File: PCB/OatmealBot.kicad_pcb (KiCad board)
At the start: 2 copper layers, 65 x 56 mm, 5 parts, among them J2 RPi_GPIO

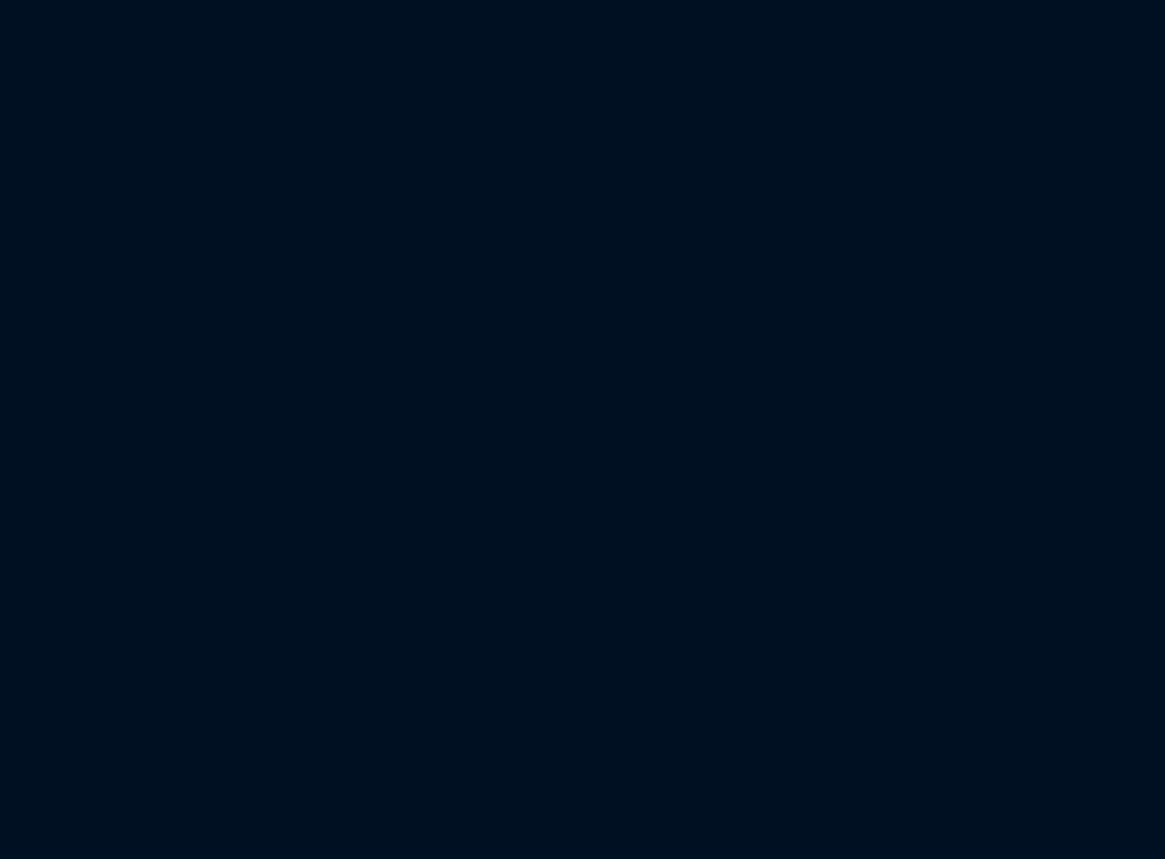
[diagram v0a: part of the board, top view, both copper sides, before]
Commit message: Started assigning some footprints. Initial PCB layout.
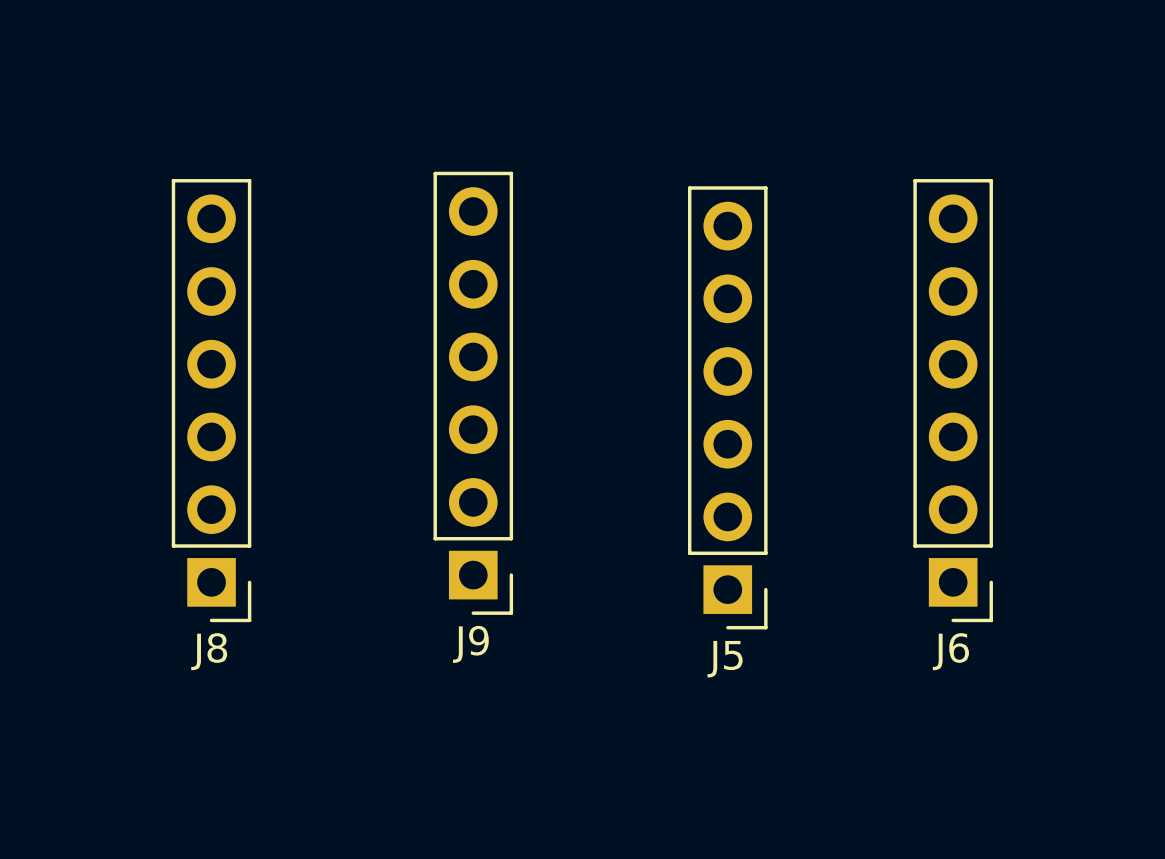
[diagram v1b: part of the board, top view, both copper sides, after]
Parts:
- added J5: Motor 3, Pin_Headers:Pin_Header_Straight_1x06_Pitch2.54mm, F.Cu at (53.3, 67.3)
- added J6: Motor 4, Pin_Headers:Pin_Header_Straight_1x06_Pitch2.54mm, F.Cu at (61.2, 67.1)
- added J8: Motor 1, Pin_Headers:Pin_Header_Straight_1x06_Pitch2.54mm, F.Cu at (35.3, 67.1)
- added J9: Motor 2, Pin_Headers:Pin_Header_Straight_1x06_Pitch2.54mm, F.Cu at (44.5, 66.8)
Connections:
- net Net-(J2-Pad1) renamed +3.3V
- net Net-(J2-Pad10) renamed PI_RXD
- net Net-(J2-Pad11) renamed Servo3
- net Net-(J2-Pad12) renamed Servo2
- net Net-(J2-Pad18) renamed OLED_RESET
- net Net-(J2-Pad19) renamed MOSI
- net Net-(J2-Pad21) renamed MISO
- net Net-(J2-Pad22) renamed OLED_DC
- net Net-(J2-Pad23) renamed SCLK
- net Net-(J2-Pad24) renamed OLED_CS
- net Net-(J2-Pad29) renamed ENC4B
- net Net-(J2-Pad31) renamed ENC4A
- net Net-(J2-Pad32) renamed Servo1
- net Net-(J2-Pad33) renamed ENC3A
- net Net-(J2-Pad35) renamed ENC3B
- net Net-(J2-Pad36) renamed ENC2A
- net Net-(J2-Pad37) renamed ENC2B
- net Net-(J2-Pad38) renamed ENC1B
- net Net-(J2-Pad40) renamed ENC1A
- net Net-(J2-Pad8) renamed PI_TXD
- J2 pad 14: Net-(J2-Pad14) -> GND
- J2 pad 2: Net-(J2-Pad2) -> +5V
- J2 pad 20: Net-(J2-Pad20) -> GND
- J2 pad 25: Net-(J2-Pad25) -> GND
- J2 pad 30: Net-(J2-Pad30) -> GND
- J2 pad 34: Net-(J2-Pad34) -> GND
- J2 pad 39: Net-(J2-Pad39) -> GND
- J2 pad 4: Net-(J2-Pad4) -> +5V
- J2 pad 6: Net-(J2-Pad6) -> GND
- J2 pad 9: Net-(J2-Pad9) -> GND

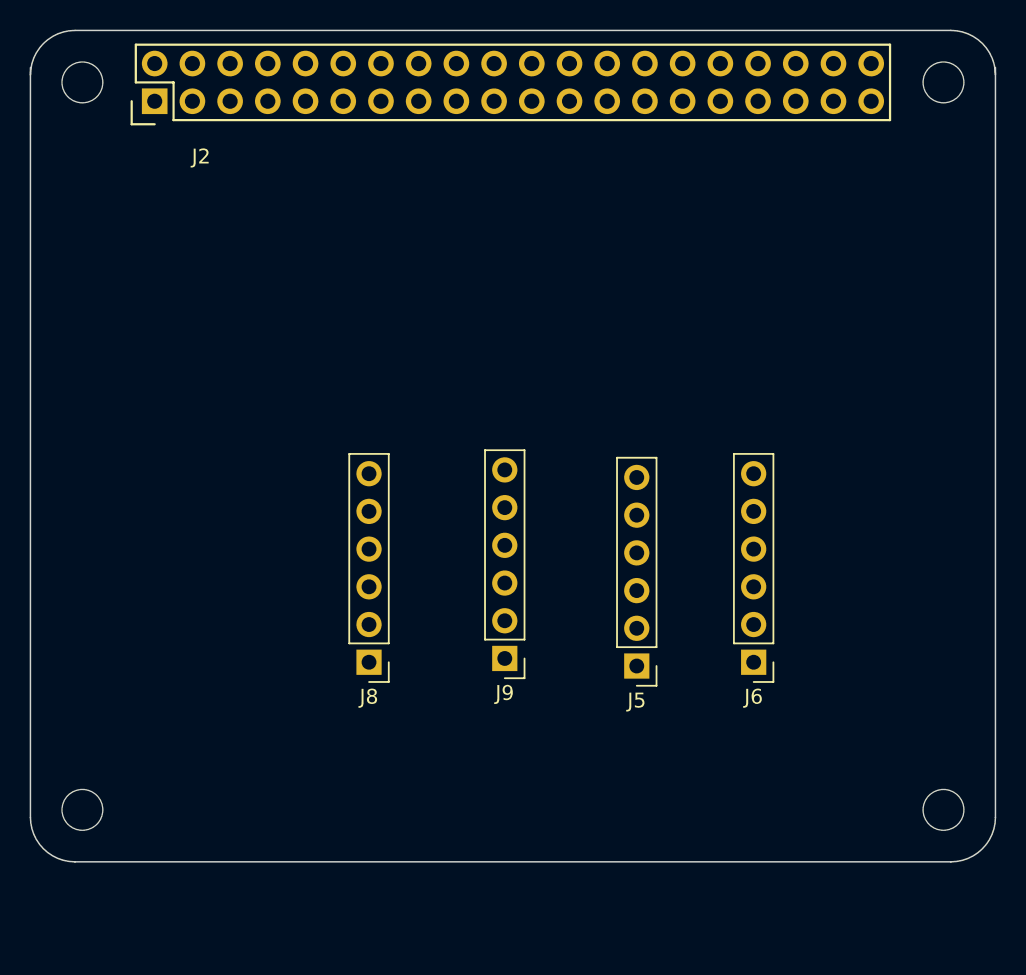
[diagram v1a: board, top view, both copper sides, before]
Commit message: Fixed PCB edges to connect properly. Removed extra explanation text about selecting the right footprint. Attempted to fix 3D models, but it hasn't worked right.
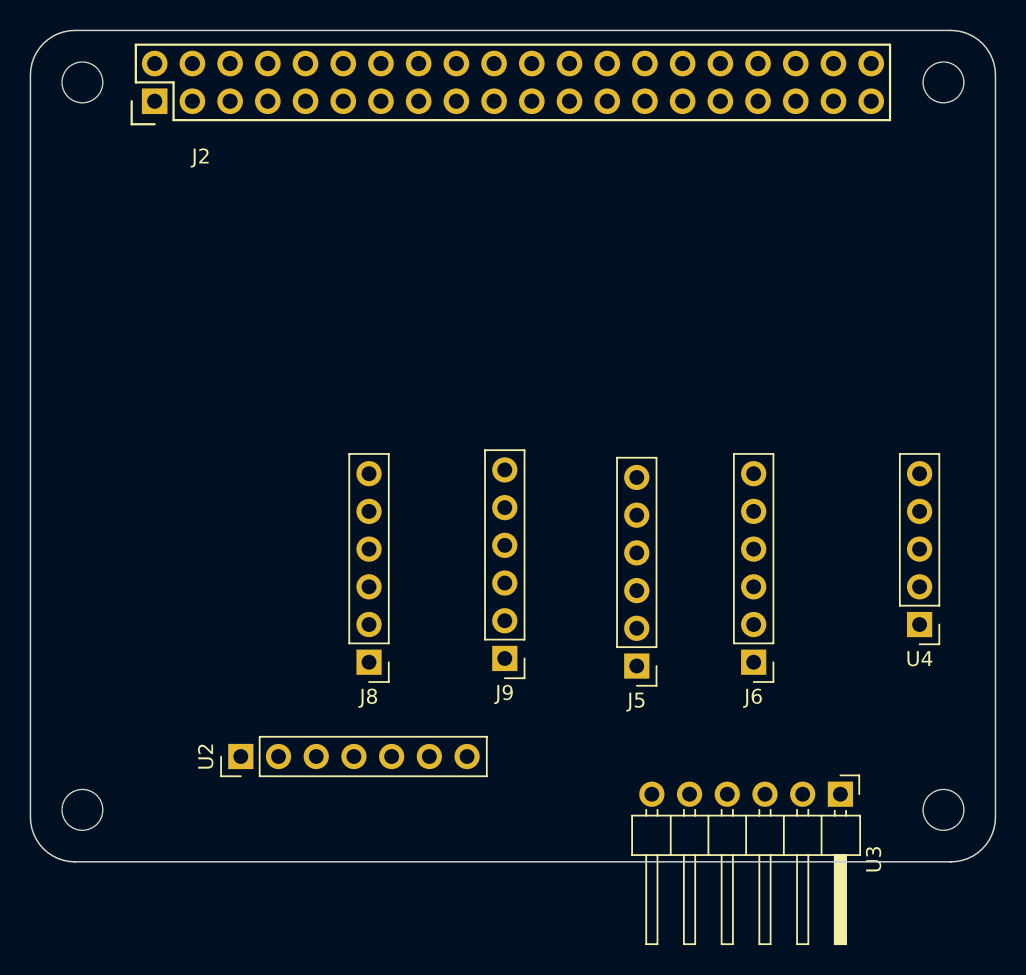
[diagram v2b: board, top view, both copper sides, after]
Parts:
- added U2: SPI_OLED, Socket_Strips:Socket_Strip_Straight_1x07_Pitch2.54mm, F.Cu at (26.7, 73.4)
- added U3: FTDI-Cable, Pin_Headers:Pin_Header_Angled_1x06_Pitch2.54mm, F.Cu at (67.1, 75.9)
- added U4: PololuD24V22F, Socket_Strips:Socket_Strip_Straight_1x05_Pitch2.54mm, F.Cu at (72.4, 64.5)
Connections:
- net Net-(J2-Pad13) renamed HighPower2
- net Net-(J2-Pad7) renamed Headlight
- J2 pad 17: Net-(J2-Pad17) -> +3.3V
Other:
- outline, holes or cut-outs redrawn
- board text removed: "Select one of these board edges depending upon the type of socket that is used."

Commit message: Fixed some of the 3D models. SPI_OLED and the Pololu power connector still aren't lined up properly though.
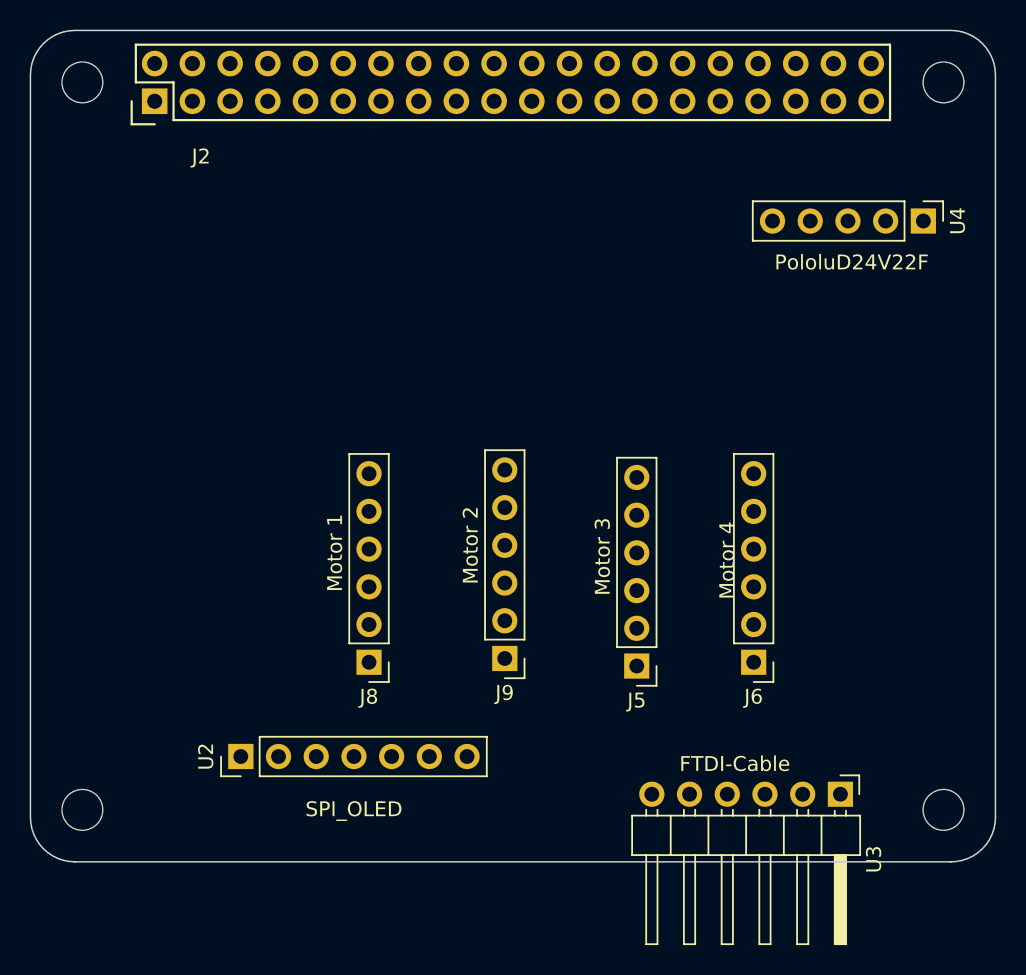
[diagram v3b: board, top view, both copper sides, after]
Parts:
- moved U4 27.2 mm to (72.6, 37.3), turned to 270 degrees
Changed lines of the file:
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@@
       (effects (font (size 1 1) (thickness 0.15)))
     )
-    (fp_text value "Motor 3" (at 0 15.03 180) (layer F.Fab)
+    (fp_text value "Motor 3" (at 2.286 7.366 270) (layer F.SilkS)
       (effects (font (size 1 1) (thickness 0.15)))
     )
@@
     (pad 6 thru_hole oval (at 0 12.7 180) (size 1.7 1.7) (drill 1) (layers *.Cu *.Mask)
       (net 33 "Net-(J5-Pad6)"))
-    (model ${KISYS3DMOD}/Pin_Headers.3dshapes/Pin_Header_Straight_1x06_Pitch2.54mm.wrl
+    (model ${KISYS3DMOD}/Connector_PinHeader_2.54mm.3dshapes/PinHeader_1x06_P2.54mm_Vertical.wrl
       (at (xyz 0 0 0))
       (scale (xyz 1 1 1))
@@
       (effects (font (size 1 1) (thickness 0.15)))
     )
-    (fp_text value "Motor 4" (at 0 15.03 180) (layer F.Fab)
+    (fp_text value "Motor 4" (at 1.778 6.858 270) (layer F.SilkS)
       (effects (font (size 1 1) (thickness 0.15)))
     )
@@
     (pad 6 thru_hole oval (at 0 12.7 180) (size 1.7 1.7) (drill 1) (layers *.Cu *.Mask)
       (net 37 "Net-(J6-Pad6)"))
-    (model ${KISYS3DMOD}/Pin_Headers.3dshapes/Pin_Header_Straight_1x06_Pitch2.54mm.wrl
+    (model ${KISYS3DMOD}/Connector_PinHeader_2.54mm.3dshapes/PinHeader_1x06_P2.54mm_Vertical.wrl
       (at (xyz 0 0 0))
       (scale (xyz 1 1 1))
@@
       (effects (font (size 1 1) (thickness 0.15)))
     )
-    (fp_text value "Motor 1" (at 0 15.03 180) (layer F.Fab)
+    (fp_text value "Motor 1" (at 2.286 7.366 270) (layer F.SilkS)
       (effects (font (size 1 1) (thickness 0.15)))
     )
@@
     (pad 6 thru_hole oval (at 0 12.7 180) (size 1.7 1.7) (drill 1) (layers *.Cu *.Mask)
       (net 41 "Net-(J8-Pad6)"))
-    (model ${KISYS3DMOD}/Pin_Headers.3dshapes/Pin_Header_Straight_1x06_Pitch2.54mm.wrl
+    (model ${KISYS3DMOD}/Connector_PinHeader_2.54mm.3dshapes/PinHeader_1x06_P2.54mm_Vertical.wrl
       (at (xyz 0 0 0))
       (scale (xyz 1 1 1))
@@
       (effects (font (size 1 1) (thickness 0.15)))
     )
-    (fp_text value "Motor 2" (at 0 15.03 180) (layer F.Fab)
+    (fp_text value "Motor 2" (at 2.286 7.62 270) (layer F.SilkS)
       (effects (font (size 1 1) (thickness 0.15)))
     )
@@
     (pad 6 thru_hole oval (at 0 12.7 180) (size 1.7 1.7) (drill 1) (layers *.Cu *.Mask)
       (net 45 "Net-(J9-Pad6)"))
-    (model ${KISYS3DMOD}/Pin_Headers.3dshapes/Pin_Header_Straight_1x06_Pitch2.54mm.wrl
+    (model ${KISYS3DMOD}/Connector_PinHeader_2.54mm.3dshapes/PinHeader_1x06_P2.54mm_Vertical.wrl
       (at (xyz 0 0 0))
       (scale (xyz 1 1 1))
@@
       (effects (font (size 1 1) (thickness 0.15)))
     )
-    (fp_text value SPI_OLED (at 0 17.57 90) (layer F.Fab)
+    (fp_text value SPI_OLED (at -3.556 7.62 180) (layer F.SilkS)
       (effects (font (size 1 1) (thickness 0.15)))
     )
@@
     (pad 7 thru_hole oval (at 0 15.24 90) (size 1.7 1.7) (drill 1) (layers *.Cu *.Mask)
       (net 20 OLED_CS))
-    (model ${KISYS3DMOD}/Socket_Strips.3dshapes/Socket_Strip_Straight_1x07_Pitch2.54mm.wrl
+    (model ${KISYS3DMOD}/Connector_PinHeader_2.54mm.3dshapes/PinHeader_1x07_P2.54mm_Vertical.wrl
       (at (xyz 0 -0.3 0))
       (scale (xyz 1 1 1))
@@
       (effects (font (size 1 1) (thickness 0.15)))
     )
-    (fp_text value FTDI-Cable (at 4.385 14.97 270) (layer F.Fab)
+    (fp_text value FTDI-Cable (at -2.032 7.112 360) (layer F.SilkS)
       (effects (font (size 1 1) (thickness 0.15)))
     )
@@
     (pad 6 thru_hole oval (at 0 12.7 270) (size 1.7 1.7) (drill 1) (layers *.Cu *.Mask)
       (net 52 "Net-(U3-Pad6)"))
-    (model ${KISYS3DMOD}/Pin_Headers.3dshapes/Pin_Header_Angled_1x06_Pitch2.54mm.wrl
+    (model ${KISYS3DMOD}/Connector_PinHeader_2.54mm.3dshapes/PinHeader_1x06_P2.54mm_Horizontal.wrl
       (at (xyz 0 0 0))
       (scale (xyz 1 1 1))
@@
   )
   (module Socket_Strips:Socket_Strip_Straight_1x05_Pitch2.54mm (layer F.Cu)
-    (at 72.39 64.516 180)
+    (at 72.644 37.338 270)
     (descr "Through hole straight socket strip, 1x05, 2.54mm pitch, single row")
     (tags "Through hole socket strip THT 1x05 2.54mm single row")
-    (fp_text reference U4 (at 0 -2.33 180) (layer F.SilkS)
-      (effects (font (size 1 1) (thickness 0.15)))
-    )
-    (fp_text value PololuD24V22F (at 0 12.49 180) (layer F.Fab)
+    (fp_text reference U4 (at 0 -2.33 270) (layer F.SilkS)
+      (effects (font (size 1 1) (thickness 0.15)))
+    )
+    (fp_text value PololuD24V22F (at 2.794 4.826 360) (layer F.SilkS)
       (effects (font (size 1 1) (thickness 0.15)))
     )
@@
     (fp_line (start 1.8 11.95) (end 1.8 -1.8) (layer F.CrtYd) (width 0.05))
     (fp_line (start 1.8 -1.8) (end -1.8 -1.8) (layer F.CrtYd) (width 0.05))
-    (fp_text user %R (at 0 -2.33 180) (layer F.Fab)
-      (effects (font (size 1 1) (thickness 0.15)))
-    )
-    (pad 1 thru_hole rect (at 0 0 180) (size 1.7 1.7) (drill 1) (layers *.Cu *.Mask)
+    (fp_text user %R (at 0 -2.33 270) (layer F.Fab)
+      (effects (font (size 1 1) (thickness 0.15)))
+    )
+    (pad 1 thru_hole rect (at 0 0 270) (size 1.7 1.7) (drill 1) (layers *.Cu *.Mask)
       (net 53 "Net-(U4-Pad1)"))
-    (pad 2 thru_hole oval (at 0 2.54 180) (size 1.7 1.7) (drill 1) (layers *.Cu *.Mask)
+    (pad 2 thru_hole oval (at 0 2.54 270) (size 1.7 1.7) (drill 1) (layers *.Cu *.Mask)
       (net 54 "Net-(U4-Pad2)"))
-    (pad 3 thru_hole oval (at 0 5.08 180) (size 1.7 1.7) (drill 1) (layers *.Cu *.Mask)
+    (pad 3 thru_hole oval (at 0 5.08 270) (size 1.7 1.7) (drill 1) (layers *.Cu *.Mask)
       (net 55 +12V))
-    (pad 4 thru_hole oval (at 0 7.62 180) (size 1.7 1.7) (drill 1) (layers *.Cu *.Mask)
-      (net 10 GND))
-    (pad 5 thru_hole oval (at 0 10.16 180) (size 1.7 1.7) (drill 1) (layers *.Cu *.Mask)
-      (net 9 +5V))
-    (model ${KISYS3DMOD}/Socket_Strips.3dshapes/Socket_Strip_Straight_1x05_Pitch2.54mm.wrl
+    (pad 4 thru_hole oval (at 0 7.62 270) (size 1.7 1.7) (drill 1) (layers *.Cu *.Mask)
+      (net 10 GND))
+    (pad 5 thru_hole oval (at 0 10.16 270) (size 1.7 1.7) (drill 1) (layers *.Cu *.Mask)
+      (net 9 +5V))
+    (model ${KISYS3DMOD}/Connector_PinSocket_2.54mm.3dshapes/PinSocket_1x05_P2.54mm_Vertical.wrl
       (at (xyz 0 -0.2 0))
       (scale (xyz 1 1 1))
